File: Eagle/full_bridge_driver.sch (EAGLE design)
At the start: 3 parts, among them IC1 L298

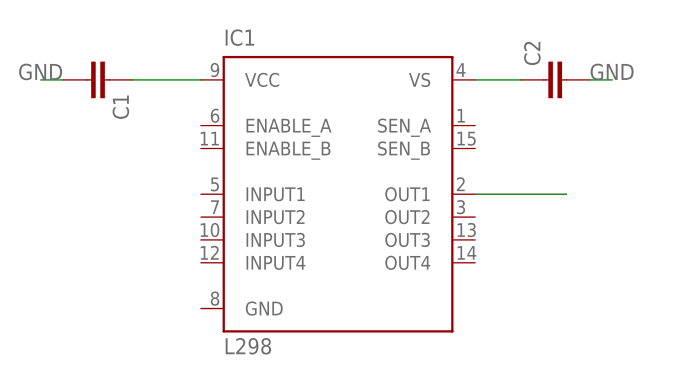
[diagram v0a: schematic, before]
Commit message: Added labels to left motor full bridge driver.
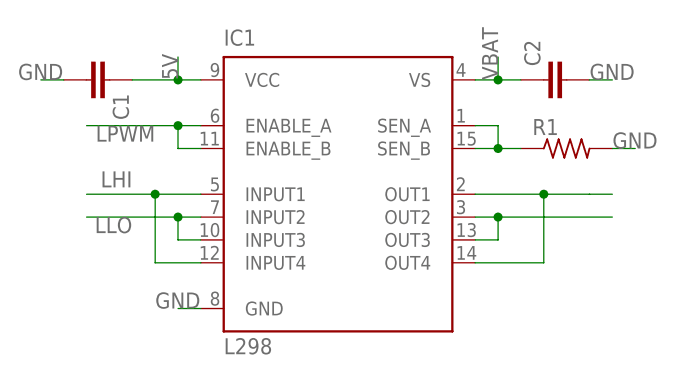
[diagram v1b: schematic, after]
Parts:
- added R1: (no value), resistor:R-US_0204/7
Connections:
- net N$1 renamed 5V
- net N$2 renamed VBAT
- new net LHI: IC1.INPUT1, IC1.INPUT4
- new net LLO: IC1.INPUT2, IC1.INPUT3
- new net LPWM: IC1.ENABLE_A, IC1.ENABLE_B
- new net N$3: IC1.OUT2, IC1.OUT3
- new net N$4: IC1.SEN_A, IC1.SEN_B, R1.1
- net GND: now also IC1.GND, R1.2
- net OUT1: now also IC1.OUT4
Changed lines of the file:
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@@
 <layer number="97" name="Info" color="7" fill="1" visible="yes" active="yes"/>
 <layer number="98" name="Guide" color="6" fill="1" visible="yes" active="yes"/>
+<layer number="99" name="SpiceOrder" color="5" fill="1" visible="yes" active="yes"/>
 </layers>
 <schematic xreflabel="%F%N/%S.%C%R" xrefpart="/%S.%C%R">
@@
 <part name="C1" library="rcl" deviceset="C-EU" device="C0603"/>
 <part name="C2" library="rcl" deviceset="C-EU" device="C0603"/>
+<part name="R1" library="resistor" deviceset="R-US_" device="0204/7"/>
 </parts>
 <sheets>
@@
 <instance part="C1" gate="G$1" x="33.02" y="76.2" rot="R270"/>
 <instance part="C2" gate="G$1" x="81.28" y="76.2" rot="R90"/>
+<instance part="R1" gate="G$1" x="83.82" y="68.58"/>
 </instances>
 <busses>
@@
 <segment>
 <pinref part="IC1" gate="L298" pin="OUT1"/>
-<wire x1="73.66" y1="63.5" x2="83.82" y2="63.5" width="0.1524" layer="91"/>
+<wire x1="73.66" y1="63.5" x2="81.28" y2="63.5" width="0.1524" layer="91"/>
+<pinref part="IC1" gate="L298" pin="OUT4"/>
+<wire x1="73.66" y1="55.88" x2="81.28" y2="55.88" width="0.1524" layer="91"/>
+<wire x1="81.28" y1="55.88" x2="81.28" y2="63.5" width="0.1524" layer="91"/>
+<junction x="81.28" y="63.5"/>
+<wire x1="81.28" y1="63.5" x2="86.36" y2="63.5" width="0.1524" layer="91"/>
+<wire x1="88.9" y1="63.5" x2="86.36" y2="63.5" width="0.1524" layer="91"/>
 </segment>
 </net>
-<net name="N$1" class="0">
+<net name="5V" class="0">
 <segment>
 <pinref part="IC1" gate="L298" pin="VCC"/>
-<wire x1="43.18" y1="76.2" x2="35.56" y2="76.2" width="0.1524" layer="91"/>
+<wire x1="43.18" y1="76.2" x2="40.64" y2="76.2" width="0.1524" layer="91"/>
 <pinref part="C1" gate="G$1" pin="1"/>
+<junction x="40.64" y="76.2"/>
+<wire x1="40.64" y1="76.2" x2="35.56" y2="76.2" width="0.1524" layer="91"/>
+<wire x1="40.64" y1="76.2" x2="40.64" y2="78.74" width="0.1524" layer="91"/>
+<label x="40.64" y="76.2" size="1.778" layer="95" rot="R90"/>
 </segment>
 </net>
-<net name="N$2" class="0">
+<net name="VBAT" class="0">
 <segment>
 <pinref part="IC1" gate="L298" pin="VS"/>
-<wire x1="73.66" y1="76.2" x2="78.74" y2="76.2" width="0.1524" layer="91"/>
+<wire x1="73.66" y1="76.2" x2="76.2" y2="76.2" width="0.1524" layer="91"/>
 <pinref part="C2" gate="G$1" pin="1"/>
+<junction x="76.2" y="76.2"/>
+<wire x1="76.2" y1="76.2" x2="78.74" y2="76.2" width="0.1524" layer="91"/>
+<wire x1="76.2" y1="76.2" x2="76.2" y2="78.74" width="0.1524" layer="91"/>
+<label x="76.2" y="76.2" size="1.778" layer="95" rot="R90"/>
 </segment>
 </net>
@@
 <label x="86.36" y="76.2" size="1.778" layer="95"/>
 </segment>
+<segment>
+<pinref part="IC1" gate="L298" pin="GND"/>
+<wire x1="43.18" y1="50.8" x2="40.64" y2="50.8" width="0.1524" layer="91"/>
+<label x="38.1" y="50.8" size="1.778" layer="95"/>
+</segment>
+<segment>
+<pinref part="R1" gate="G$1" pin="2"/>
+<wire x1="88.9" y1="68.58" x2="91.44" y2="68.58" width="0.1524" layer="91"/>
+<label x="88.9" y="68.58" size="1.778" layer="95"/>
+</segment>
 </net>
+<net name="N$4" class="0">
+<segment>
+<pinref part="IC1" gate="L298" pin="SEN_B"/>
+<wire x1="73.66" y1="68.58" x2="76.2" y2="68.58" width="0.1524" layer="91"/>
+<pinref part="R1" gate="G$1" pin="1"/>
+<wire x1="76.2" y1="68.58" x2="78.74" y2="68.58" width="0.1524" layer="91"/>
+<wire x1="76.2" y1="68.58" x2="76.2" y2="71.12" width="0.1524" layer="91"/>
+<pinref part="IC1" gate="L298" pin="SEN_A"/>
+<wire x1="76.2" y1="71.12" x2="73.66" y2="71.12" width="0.1524" layer="91"/>
+<junction x="76.2" y="68.58"/>
+</segment>
+</net>
+<net name="N$3" class="0">
+<segment>
+<pinref part="IC1" gate="L298" pin="OUT2"/>
+<wire x1="73.66" y1="60.96" x2="76.2" y2="60.96" width="0.1524" layer="91"/>
+<wire x1="76.2" y1="60.96" x2="76.2" y2="58.42" width="0.1524" layer="91"/>
+<pinref part="IC1" gate="L298" pin="OUT3"/>
+<wire x1="76.2" y1="58.42" x2="73.66" y2="58.42" width="0.1524" layer="91"/>
+<junction x="76.2" y="60.96"/>
+<wire x1="76.2" y1="60.96" x2="88.9" y2="60.96" width="0.1524" layer="91"/>
+</segment>
+</net>
+<net name="LLO" class="0">
+<segment>
+<pinref part="IC1" gate="L298" pin="INPUT2"/>
+<wire x1="43.18" y1="60.96" x2="40.64" y2="60.96" width="0.1524" layer="91"/>
+<pinref part="IC1" gate="L298" pin="INPUT3"/>
+<wire x1="40.64" y1="60.96" x2="30.48" y2="60.96" width="0.1524" layer="91"/>
+<wire x1="43.18" y1="58.42" x2="40.64" y2="58.42" width="0.1524" layer="91"/>
+<wire x1="40.64" y1="58.42" x2="40.64" y2="60.96" width="0.1524" layer="91"/>
+<junction x="40.64" y="60.96"/>
+<label x="35.56" y="60.96" size="1.778" layer="95" rot="R180"/>
+</segment>
+</net>
+<net name="LHI" class="0">
+<segment>
+<pinref part="IC1" gate="L298" pin="INPUT1"/>
+<wire x1="43.18" y1="63.5" x2="38.1" y2="63.5" width="0.1524" layer="91"/>
+<pinref part="IC1" gate="L298" pin="INPUT4"/>
+<wire x1="38.1" y1="63.5" x2="30.48" y2="63.5" width="0.1524" layer="91"/>
+<wire x1="43.18" y1="55.88" x2="38.1" y2="55.88" width="0.1524" layer="91"/>
+<wire x1="38.1" y1="55.88" x2="38.1" y2="63.5" width="0.1524" layer="91"/>
+<junction x="38.1" y="63.5"/>
+<label x="35.56" y="66.04" size="1.778" layer="95" rot="R180"/>
+</segment>
+</net>
+<net name="LPWM" class="0">
+<segment>
+<pinref part="IC1" gate="L298" pin="ENABLE_A"/>
+<wire x1="43.18" y1="71.12" x2="40.64" y2="71.12" width="0.1524" layer="91"/>
+<pinref part="IC1" gate="L298" pin="ENABLE_B"/>
+<wire x1="40.64" y1="71.12" x2="30.48" y2="71.12" width="0.1524" layer="91"/>
+<wire x1="43.18" y1="68.58" x2="40.64" y2="68.58" width="0.1524" layer="91"/>
+<wire x1="40.64" y1="68.58" x2="40.64" y2="71.12" width="0.1524" layer="91"/>
+<junction x="40.64" y="71.12"/>
+<label x="38.1" y="71.12" size="1.778" layer="95" rot="R180"/>
+</segment>
+</net>

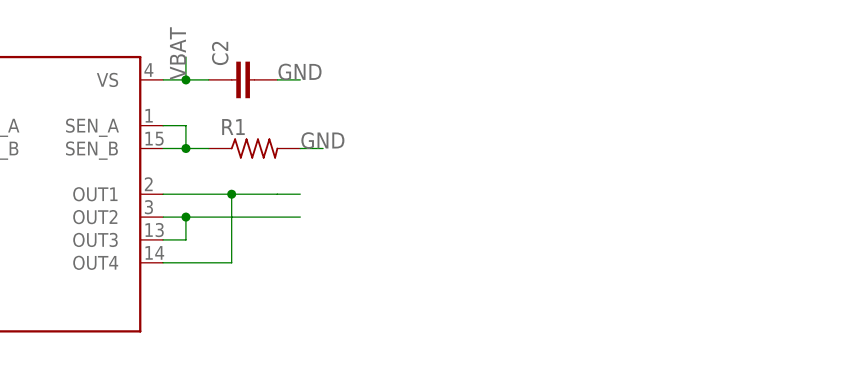
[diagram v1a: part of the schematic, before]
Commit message: Redrew motor and full bridge circuit from L298 data sheet
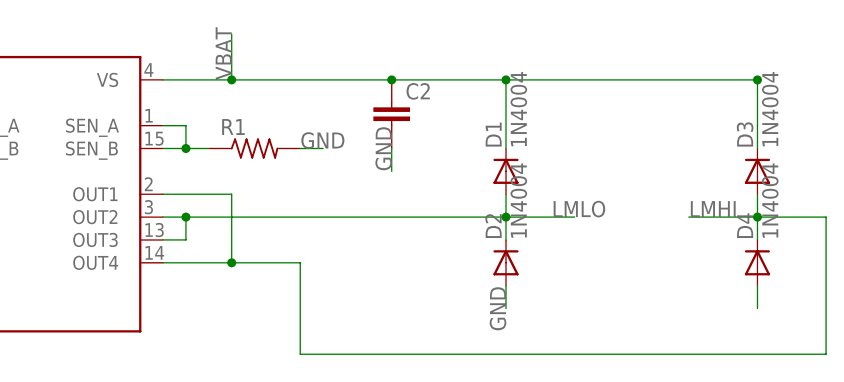
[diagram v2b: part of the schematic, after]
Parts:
- added D1, D2, D3, D4: 1N4004, diode:1N4004
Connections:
- removed net N$3: IC1.OUT2, IC1.OUT3
- removed net OUT1: IC1.OUT1, IC1.OUT4
- new net LMHI: D3.A, D4.C, IC1.OUT1, IC1.OUT4
- new net LMLO: D1.A, D2.C, IC1.OUT2, IC1.OUT3
- new net N$2: D4.A
- net GND: now also D2.A
- net VBAT: now also D1.C, D3.C
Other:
- moved on the sheet: C2
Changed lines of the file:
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@@
 <part name="C2" library="rcl" deviceset="C-EU" device="C0603"/>
 <part name="R1" library="resistor" deviceset="R-US_" device="0204/7"/>
+<part name="D1" library="diode" deviceset="1N4004" device=""/>
+<part name="D2" library="diode" deviceset="1N4004" device=""/>
+<part name="D3" library="diode" deviceset="1N4004" device=""/>
+<part name="D4" library="diode" deviceset="1N4004" device=""/>
 </parts>
 <sheets>
@@
 <instance part="IC1" gate="L298" x="58.42" y="60.96"/>
 <instance part="C1" gate="G$1" x="33.02" y="76.2" rot="R270"/>
-<instance part="C2" gate="G$1" x="81.28" y="76.2" rot="R90"/>
+<instance part="C2" gate="G$1" x="99.06" y="73.66"/>
 <instance part="R1" gate="G$1" x="83.82" y="68.58"/>
+<instance part="D1" gate="1" x="111.76" y="66.04" rot="R90"/>
+<instance part="D2" gate="1" x="111.76" y="55.88" rot="R90"/>
+<instance part="D3" gate="1" x="139.7" y="66.04" rot="R90"/>
+<instance part="D4" gate="1" x="139.7" y="55.88" rot="R90"/>
 </instances>
 <busses>
 </busses>
 <nets>
-<net name="OUT1" class="0">
+<net name="LMHI" class="0">
 <segment>
 <pinref part="IC1" gate="L298" pin="OUT1"/>
@@
 <wire x1="73.66" y1="55.88" x2="81.28" y2="55.88" width="0.1524" layer="91"/>
 <wire x1="81.28" y1="55.88" x2="81.28" y2="63.5" width="0.1524" layer="91"/>
-<junction x="81.28" y="63.5"/>
-<wire x1="81.28" y1="63.5" x2="86.36" y2="63.5" width="0.1524" layer="91"/>
-<wire x1="88.9" y1="63.5" x2="86.36" y2="63.5" width="0.1524" layer="91"/>
+<junction x="81.28" y="55.88"/>
+<wire x1="81.28" y1="55.88" x2="88.9" y2="55.88" width="0.1524" layer="91"/>
+<wire x1="88.9" y1="55.88" x2="88.9" y2="45.72" width="0.1524" layer="91"/>
+<wire x1="88.9" y1="45.72" x2="147.32" y2="45.72" width="0.1524" layer="91"/>
+<wire x1="147.32" y1="45.72" x2="147.32" y2="60.96" width="0.1524" layer="91"/>
+<pinref part="D3" gate="1" pin="A"/>
+<wire x1="139.7" y1="63.5" x2="139.7" y2="60.96" width="0.1524" layer="91"/>
+<wire x1="139.7" y1="60.96" x2="139.7" y2="58.42" width="0.1524" layer="91"/>
+<wire x1="132.08" y1="60.96" x2="139.7" y2="60.96" width="0.1524" layer="91"/>
+<junction x="139.7" y="60.96"/>
+<pinref part="D4" gate="1" pin="C"/>
+<wire x1="139.7" y1="60.96" x2="147.32" y2="60.96" width="0.1524" layer="91"/>
+<label x="132.08" y="60.96" size="1.778" layer="95"/>
 </segment>
 </net>
@@
 </segment>
 </net>
-<net name="VBAT" class="0">
-<segment>
-<pinref part="IC1" gate="L298" pin="VS"/>
-<wire x1="73.66" y1="76.2" x2="76.2" y2="76.2" width="0.1524" layer="91"/>
-<pinref part="C2" gate="G$1" pin="1"/>
-<junction x="76.2" y="76.2"/>
-<wire x1="76.2" y1="76.2" x2="78.74" y2="76.2" width="0.1524" layer="91"/>
-<wire x1="76.2" y1="76.2" x2="76.2" y2="78.74" width="0.1524" layer="91"/>
-<label x="76.2" y="76.2" size="1.778" layer="95" rot="R90"/>
-</segment>
-</net>
 <net name="GND" class="0">
 <segment>
@@
 <wire x1="27.94" y1="76.2" x2="25.4" y2="76.2" width="0.1524" layer="91"/>
 <label x="22.86" y="76.2" size="1.778" layer="95"/>
-</segment>
-<segment>
-<pinref part="C2" gate="G$1" pin="2"/>
-<wire x1="86.36" y1="76.2" x2="88.9" y2="76.2" width="0.1524" layer="91"/>
-<label x="86.36" y="76.2" size="1.778" layer="95"/>
 </segment>
 <segment>
@@
 <wire x1="88.9" y1="68.58" x2="91.44" y2="68.58" width="0.1524" layer="91"/>
 <label x="88.9" y="68.58" size="1.778" layer="95"/>
+</segment>
+<segment>
+<pinref part="C2" gate="G$1" pin="2"/>
+<wire x1="99.06" y1="68.58" x2="99.06" y2="66.04" width="0.1524" layer="91"/>
+<label x="99.06" y="66.04" size="1.778" layer="95" rot="R90"/>
+</segment>
+<segment>
+<pinref part="D2" gate="1" pin="A"/>
+<wire x1="111.76" y1="53.34" x2="111.76" y2="50.8" width="0.1524" layer="91"/>
+<label x="111.76" y="48.26" size="1.778" layer="95" rot="R90"/>
 </segment>
 </net>
@@
 </segment>
 </net>
-<net name="N$3" class="0">
+<net name="LMLO" class="0">
 <segment>
 <pinref part="IC1" gate="L298" pin="OUT2"/>
@@
 <wire x1="76.2" y1="58.42" x2="73.66" y2="58.42" width="0.1524" layer="91"/>
 <junction x="76.2" y="60.96"/>
-<wire x1="76.2" y1="60.96" x2="88.9" y2="60.96" width="0.1524" layer="91"/>
+<wire x1="76.2" y1="60.96" x2="111.76" y2="60.96" width="0.1524" layer="91"/>
+<pinref part="D1" gate="1" pin="A"/>
+<wire x1="111.76" y1="63.5" x2="111.76" y2="60.96" width="0.1524" layer="91"/>
+<junction x="111.76" y="60.96"/>
+<wire x1="111.76" y1="60.96" x2="111.76" y2="58.42" width="0.1524" layer="91"/>
+<pinref part="D2" gate="1" pin="C"/>
+<wire x1="111.76" y1="60.96" x2="119.38" y2="60.96" width="0.1524" layer="91"/>
+<label x="116.84" y="60.96" size="1.778" layer="95"/>
 </segment>
 </net>
@@
 </segment>
 </net>
+<net name="VBAT" class="0">
+<segment>
+<pinref part="C2" gate="G$1" pin="1"/>
+<pinref part="IC1" gate="L298" pin="VS"/>
+<wire x1="73.66" y1="76.2" x2="81.28" y2="76.2" width="0.1524" layer="91"/>
+<wire x1="81.28" y1="76.2" x2="99.06" y2="76.2" width="0.1524" layer="91"/>
+<wire x1="99.06" y1="76.2" x2="111.76" y2="76.2" width="0.1524" layer="91"/>
+<junction x="81.28" y="76.2"/>
+<junction x="99.06" y="76.2"/>
+<wire x1="81.28" y1="76.2" x2="81.28" y2="81.28" width="0.1524" layer="91"/>
+<label x="81.28" y="76.2" size="1.778" layer="95" rot="R90"/>
+<pinref part="D1" gate="1" pin="C"/>
+<wire x1="111.76" y1="76.2" x2="111.76" y2="68.58" width="0.1524" layer="91"/>
+<junction x="111.76" y="76.2"/>
+<wire x1="111.76" y1="76.2" x2="139.7" y2="76.2" width="0.1524" layer="91"/>
+<wire x1="139.7" y1="76.2" x2="139.7" y2="71.12" width="0.1524" layer="91"/>
+<pinref part="D3" gate="1" pin="C"/>
+<wire x1="139.7" y1="68.58" x2="139.7" y2="71.12" width="0.1524" layer="91"/>
+<junction x="139.7" y="76.2"/>
+</segment>
+</net>
+<net name="N$2" class="0">
+<segment>
+<pinref part="D4" gate="1" pin="A"/>
+<wire x1="139.7" y1="53.34" x2="139.7" y2="50.8" width="0.1524" layer="91"/>
+</segment>
+</net>

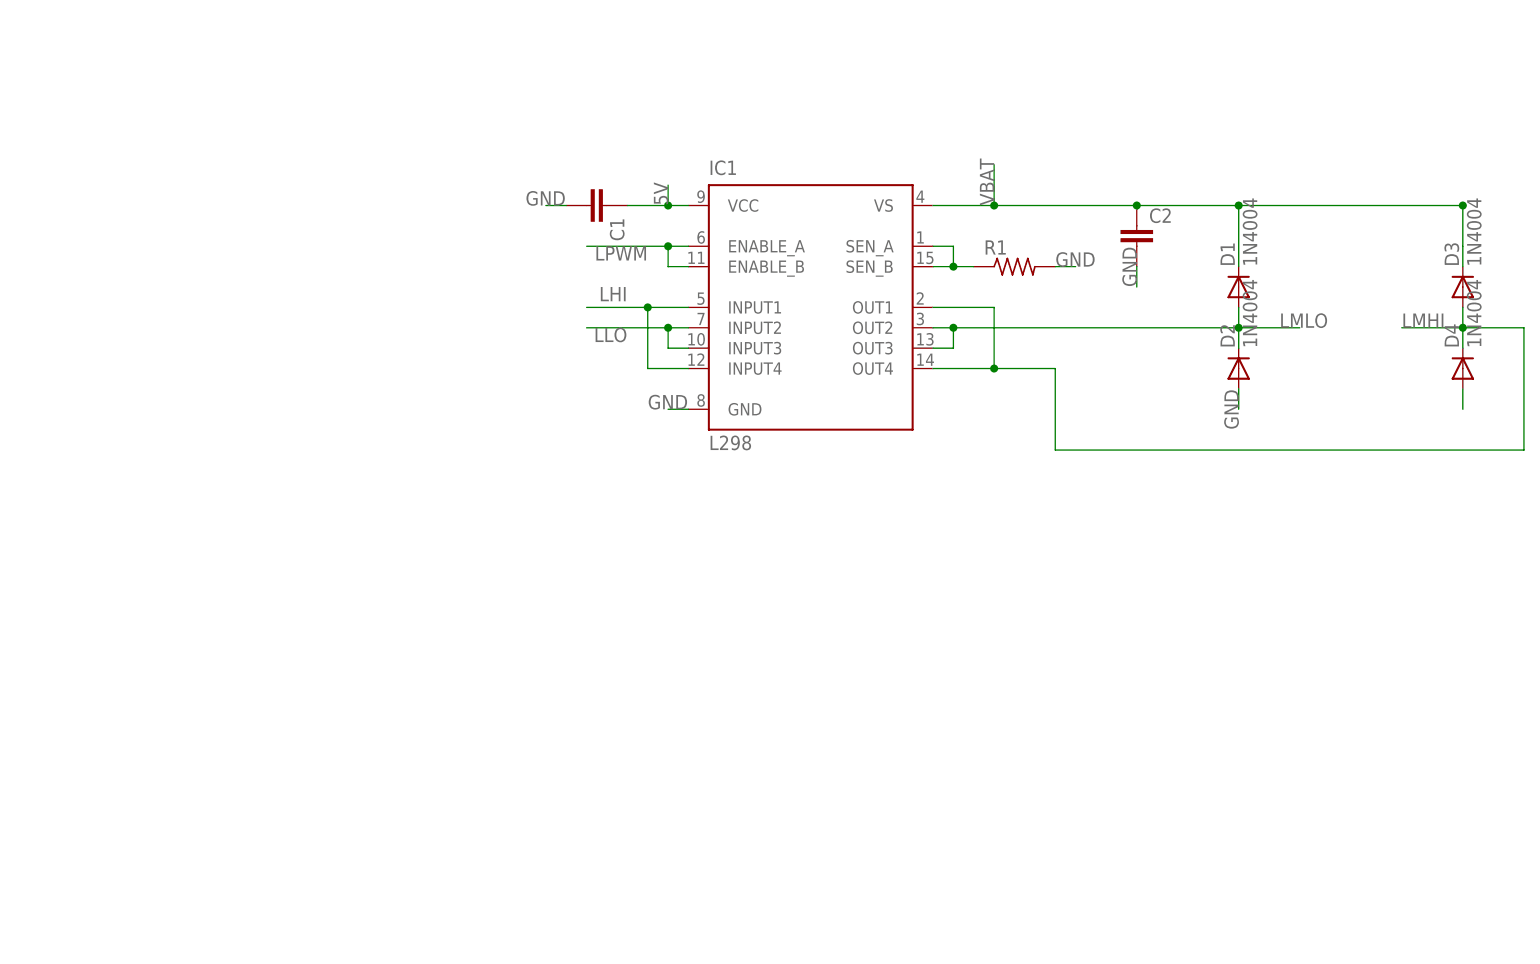
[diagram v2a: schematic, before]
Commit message: Added 5V voltage regulator to full bridge schematic.
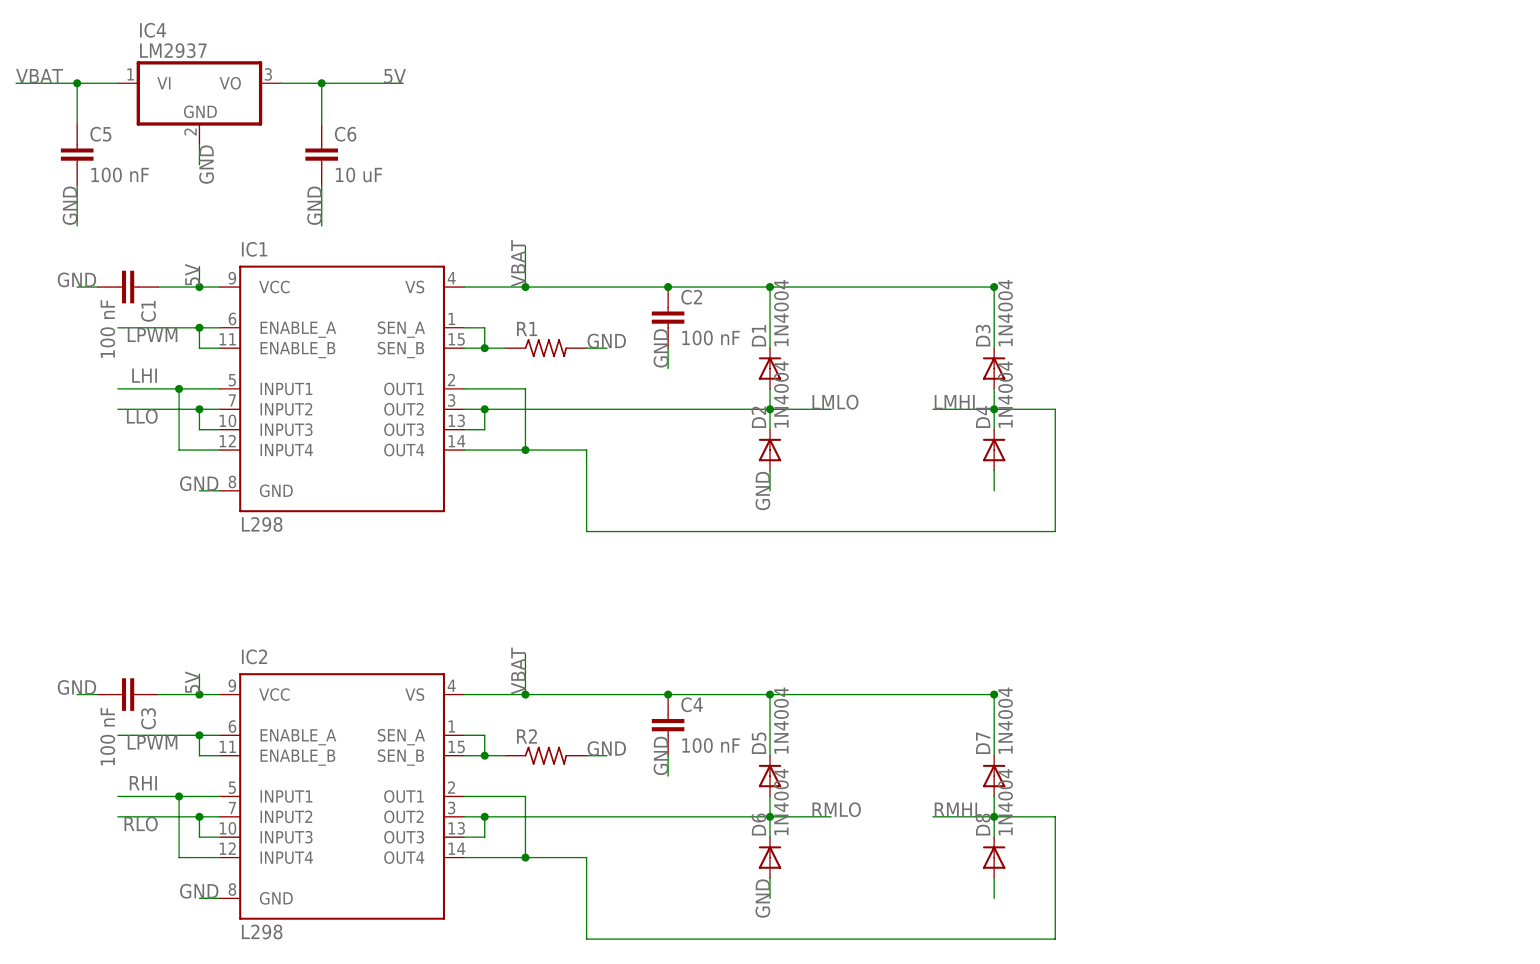
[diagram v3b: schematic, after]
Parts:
- added C3, C4, C5: 100 nF, rcl:C-EUC0603
- added C6: 10 uF, rcl:C-EUC0603
- added D5, D6, D7, D8: 1N4004, diode:1N4004
- added IC2: L298, st-microelectronics:L298
- added IC4: LM2937, linear:LM2937
- added R2: (no value), resistor:R-US_0204/7
- C1, C2: value (none) -> 100 nF
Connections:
- new net N$1: IC2.SEN_A, IC2.SEN_B, R2.1
- new net N$3: D8.A
- new net RHI: IC2.INPUT1, IC2.INPUT4
- new net RLO: IC2.INPUT2, IC2.INPUT3
- new net RMHI: D7.A, D8.C, IC2.OUT1, IC2.OUT4
- new net RMLO: D5.A, D6.C, IC2.OUT2, IC2.OUT3
- net 5V: now also C3.1, C6.1, IC2.VCC, IC4.VO
- net GND: now also C3.2, C4.2, C5.2, C6.2, D6.A, IC2.GND, IC4.GND, R2.2
- net LPWM: now also IC2.ENABLE_A, IC2.ENABLE_B
- net VBAT: now also C4.1, C5.1, D5.C, D7.C, IC2.VS, IC4.VI
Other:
- moved on the sheet: C1, C2, D1, D2, D3, D4, IC1, R1

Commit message: Updated full bridge schematic a while ago
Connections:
- removed net N$2: D4.A
- removed net N$3: D8.A
- net GND: now also D4.A, D8.A
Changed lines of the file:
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@@
 <label x="-2.54" y="73.66" size="1.778" layer="95" rot="R90"/>
+</segment>
+<segment>
+<pinref part="D8" gate="1" pin="A"/>
+<wire x1="81.28" y1="-7.62" x2="81.28" y2="-10.16" width="0.1524" layer="91"/>
+<label x="81.28" y="-12.7" size="1.778" layer="95" rot="R90"/>
+</segment>
+<segment>
+<pinref part="D4" gate="1" pin="A"/>
+<wire x1="81.28" y1="43.18" x2="81.28" y2="40.64" width="0.1524" layer="91"/>
+<label x="81.28" y="38.1" size="1.778" layer="95" rot="R90"/>
 </segment>
 </net>
@@
 </segment>
 </net>
-<net name="N$2" class="0">
-<segment>
-<pinref part="D4" gate="1" pin="A"/>
-<wire x1="81.28" y1="43.18" x2="81.28" y2="40.64" width="0.1524" layer="91"/>
-</segment>
-</net>
 <net name="N$1" class="0">
 <segment>
@@
 </segment>
 </net>
-<net name="N$3" class="0">
-<segment>
-<pinref part="D8" gate="1" pin="A"/>
-<wire x1="81.28" y1="-7.62" x2="81.28" y2="-10.16" width="0.1524" layer="91"/>
-</segment>
-</net>
